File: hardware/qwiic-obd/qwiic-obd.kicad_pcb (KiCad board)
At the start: 2 copper layers, 161 parts, among them J101 I2C_STANDARD, J102 DB15_Female_HighDensity, J103 I2C_STANDARD, J601 PIC-ICSPPOLAR_LOCK, Q201 2N7002, Q202 2N7002, Q203 2N7002, Q301 2N7002, Q501 DMG2301L, Q502 DMG2301L, Q503 MMBT3906, Q504 DMG2301L, Q601 DMG2301L, Q602 2N7002, Q603 2N7002, Q604 2N7002, Q605 2N7002, Q606 2N7002, Q607 2N7002, Q608 2N7002, Q701 2N7002, Q702 2N7002, Q703 2N7002, Q704 MMBT3904, SW401 SW_Push, U201 TS5A3359DCUR, U202 TS5A3359DCUR, U203 TS5A3359DCUR, U301 TH8056KDC-AAA-008-RE, U302 MCP2557FD-xMF, U401 TCA9534, U402 MCP3423, U403 TCA9534, U404 ADM6320BX33ARJZ-R7, U405 TCA9534, U501 AP63203WU, U502 XC9142B50CMR-G, U601 LM317L_SOT-89, U602 NCS20072, U603 PIC16F15225-I/ST, U701 NCS20072, U702 SC16IS741A, U801 SC18IS602BIPW_128, U802 MCP2515-xST, X701 ASV-12.000MHZ-EJ-T, X801 ASV-12.000MHZ-EJ-T

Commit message: OK, layout v1 complete
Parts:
- removed the R301 at (127.9, 133.0)
- removed the R302 at (134.4, 123.1)
- removed R306, R409, R802, R803: 10k, Resistor_SMD:R_0805_2012Metric_Pad1.20x1.40mm_HandSolder
- removed the R617 at (189.2, 42.7)
- removed the R710 at (187.9, 70.8)
- removed U405: TCA9534, Package_SO:TSSOP-16_4.4x5mm_P0.65mm
- added J401: 1x4, Connector_PinSocket_2.54mm:PinSocket_1x04_P2.54mm_Vertical, F.Cu at (151.4, 41.2)
- added Q607: 2N7002, Package_TO_SOT_SMD:SOT-23, F.Cu at (106.7, 33.4)
- added R609: 10k, Resistor_SMD:R_0805_2012Metric_Pad1.20x1.40mm_HandSolder, B.Cu at (105.7, 32.5)
- added U204: TS5A3359DCUR, UltraLibrarian:TS5A3359DCUR, F.Cu at (55.9, 55.9)
- added U205: TS5A3359DCUR, UltraLibrarian:TS5A3359DCUR, F.Cu at (69.1, 63.5)
- C302, C503, C506, C507, C511, C604, C801, D101, D102, D103, D104, D105, D601, D604, D605, D701, Q301, Q504, Q601, R202, R204, R206, R505, R601, R701, R702, R703, R704, R706: moved to B.Cu
- Q609: renamed from Q608; moved to B.Cu
- R303: renamed from R305; moved to B.Cu
- R614: renamed from R613; moved to B.Cu
- R616: renamed from R615; moved to B.Cu
- R617: renamed from R616; moved to B.Cu
- RN403: footprint UltraLibrarian:742C163103JP -> Resistor_THT:R_Array_SIP5
- moved X801 131.6 mm to (81.8, 66.0), turned to 90 degrees
- moved L501 125.8 mm to (47.2, 21.8), turned to -90 degrees
- moved R801 124.1 mm to (94.5, 53.3)
- moved C801 120.6 mm to (88.9, 55.4), turned to 90 degrees
- moved Q501 117.7 mm to (60.4, 22.4)
- moved C508 117.0 mm to (46.2, 25.9), turned to -90 degrees
- moved C511 116.9 mm to (52.3, 23.9)
- moved U501 115.9 mm to (49.8, 21.8), turned to 90 degrees
- moved R501 114.2 mm to (54.4, 29.0), turned to -90 degrees
- moved C507 114.1 mm to (50.3, 19.8), turned to 180 degrees
- moved R505 114.0 mm to (52.3, 21.8)
- moved C509 113.8 mm to (48.3, 25.9), turned to -90 degrees
- moved Q504 113.3 mm to (48.3, 22.8), turned to 90 degrees
- moved C516 113.2 mm to (85.9, 24.9), turned to 90 degrees
- moved U802 112.7 mm to (86.4, 57.9)
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- renumbered Q607 to Q608, R303 to R301, R304 to R302, R307 to R304, R308 to R305, R609 to R610, R610 to R611, R611 to R612, R612 to R613, R614 to R615, R711 to R710
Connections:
- C302 pad 2: +5V_SW -> +5V
- C514 pad 2: +3V3 -> +5V
- C515 pad 1: +3V3 -> +5V
- C516 pad 1: +3V3 -> +5V
- C601 pad 2: VBAT -> +12V
- J102 pad 3: MS_CAN_HIGH -> MS_CAN_HI
- J102 pad 6: HS_CAN_HIGH -> HS_CAN_HI
- R506 pad 1: +3V3 -> +5V
- R614 pad 1: +5V_SW -> +5V
- RN402 pad 1: +3V3_NOSW -> ~{CAN_RX0BF}
- RN402 pad 10: Net-(RN402-Pad10) -> +3V3_NOSW
- RN402 pad 11: Net-(RN402-Pad11) -> +3V3_NOSW
- RN402 pad 12: ~{CAN_TX2RTS} -> +3V3_NOSW
- RN402 pad 13: ~{CAN_TX1RTS} -> +3V3_NOSW
- RN402 pad 14: ~{CAN_TX0RTS} -> +3V3_NOSW
- RN402 pad 15: ~{CAN_RX1BF} -> +3V3_NOSW
- RN402 pad 16: ~{CAN_RX0BF} -> +3V3_NOSW
- RN402 pad 2: +3V3_NOSW -> ~{CAN_RX1BF}
- RN402 pad 3: +3V3_NOSW -> ~{CAN_TX0RTS}
- RN402 pad 4: +3V3_NOSW -> ~{CAN_TX1RTS}
- RN402 pad 5: +3V3_NOSW -> ~{CAN_TX2RTS}
- RN402 pad 6: +3V3_NOSW -> Net-(RN402-Pad6)
- RN402 pad 7: +3V3_NOSW -> ~{RESET}
- RN402 pad 8: GND -> CAN_SOF
- RN402 pad 9: CAN_SOF -> GND
- RN403 pad 2: +3V3_NOSW -> ~{CAN_INT}
- RN403 pad 3: +3V3_NOSW -> ~{UART_INT}
- RN403 pad 4: +3V3_NOSW -> ~{SPI_INT}
- RN403 pad 5: +3V3_NOSW -> ~{J1850_INT}
- U202 pad 1: MUX_CAN_RX -> HS_CAN_HI
- U202 pad 2: MUX_CAN_RX -> MS_CAN_HI
- U202 pad 3: SW_CAN_RX -> unconnected-(U202-Pad3)
- U202 pad 7: CAN_RX -> CAN_HI
- U202 pad 8: +3V3 -> +5V
- U203 pad 1: ~{MUX_CAN_EN} -> MUX_CAN_RX
- U203 pad 2: ~{MUX_CAN_EN} -> MUX_CAN_RX
- U203 pad 3: unconnected-(U203-Pad3) -> SW_CAN_RX
- U203 pad 7: ~{CAN_EN} -> CAN_RX
- U302 pad 3: +5V_SW -> +5V
- U403 pad 10: Net-(RN402-Pad11) -> Net-(RN402-Pad6)
- U403 pad 11: Net-(RN402-Pad10) -> ~{RESET}
- U502 pad 4: +3V3 -> +5V
- U601 pad 3: VBAT -> +12V
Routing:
- net +3V3_NOSW: track 0.00 -> 189.6 mm, vias 0 -> 9
- net SDA: track 0.00 -> 183.1 mm, vias 0 -> 15
- net SCL: track 0.00 -> 182.9 mm, vias 0 -> 14
- net GND: track 0.00 -> 166.1 mm, vias 0 -> 53
- net +12V: track 0.00 -> 150.3 mm, vias 0 -> 7
- net ~{RESET}: track 0.00 -> 145.3 mm, vias 0 -> 8
- net CAN_SEL1: track 0.00 -> 99.9 mm, vias 0 -> 8
- net CAN_SEL0: track 0.00 -> 96.7 mm, vias 0 -> 8
- net J1850_BUS+: track 0.00 -> 96.4 mm, vias 0 -> 7
- net ~{CAN_INT}: track 0.00 -> 89.8 mm, vias 0 -> 5
- net PWR_CTRL: track 0.00 -> 88.3 mm, vias 0 -> 7
- net J1850_BUS-: track 0.00 -> 88.0 mm, vias 0 -> 10
- net ~{SPI_INT}: track 0.00 -> 78.9 mm, vias 0 -> 5
- net +3V3: track 0.00 -> 77.5 mm, vias 0 -> 27
- net SAE_PWM: track 0.00 -> 75.4 mm, vias 0 -> 6
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- added copper zone on In2.Cu, net +3V3
- added copper zone on In1.Cu, net +3V3_NOSW
- added copper zone on In1.Cu, net +5V
- added copper zone on B.Cu, net GND
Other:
- board outline added: 109.9 x 52.7 mm
- copper layers 2 -> 4

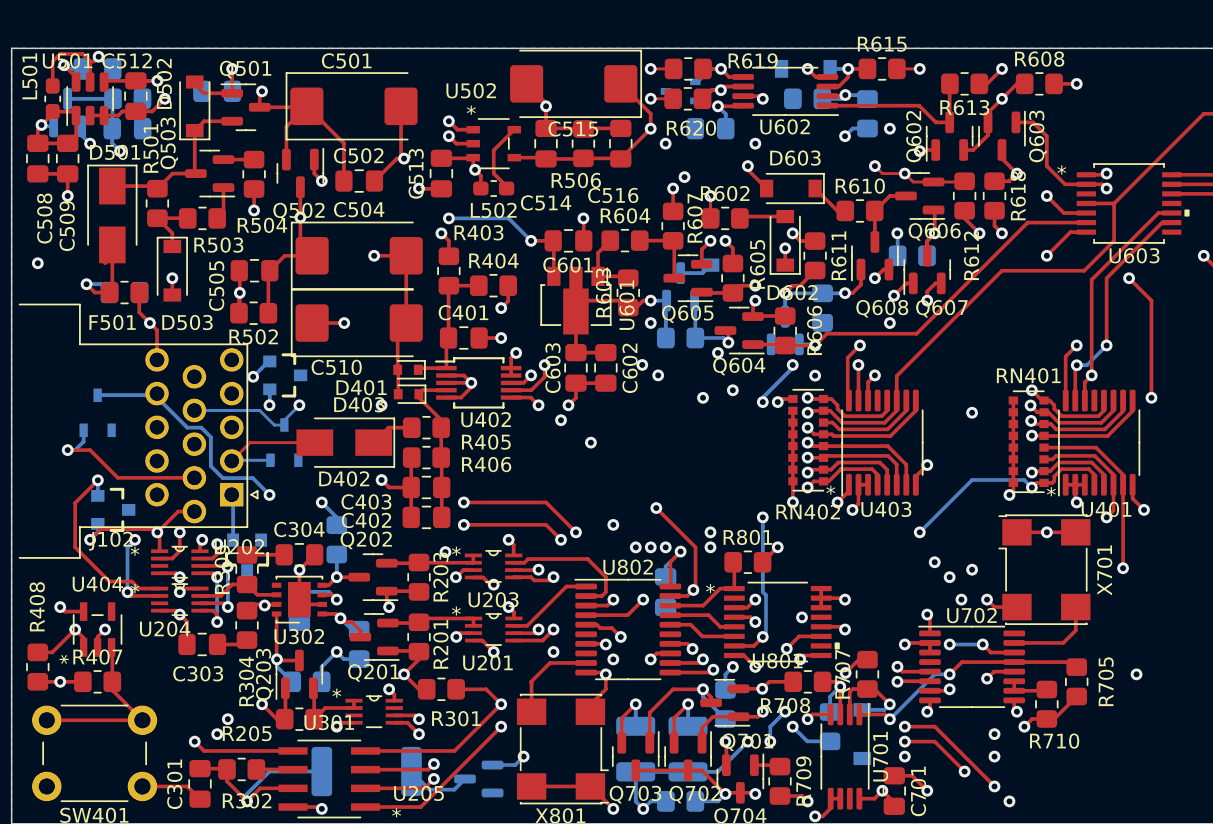
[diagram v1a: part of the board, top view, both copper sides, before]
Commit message: Get it all connected (had a few unrouted glitches)
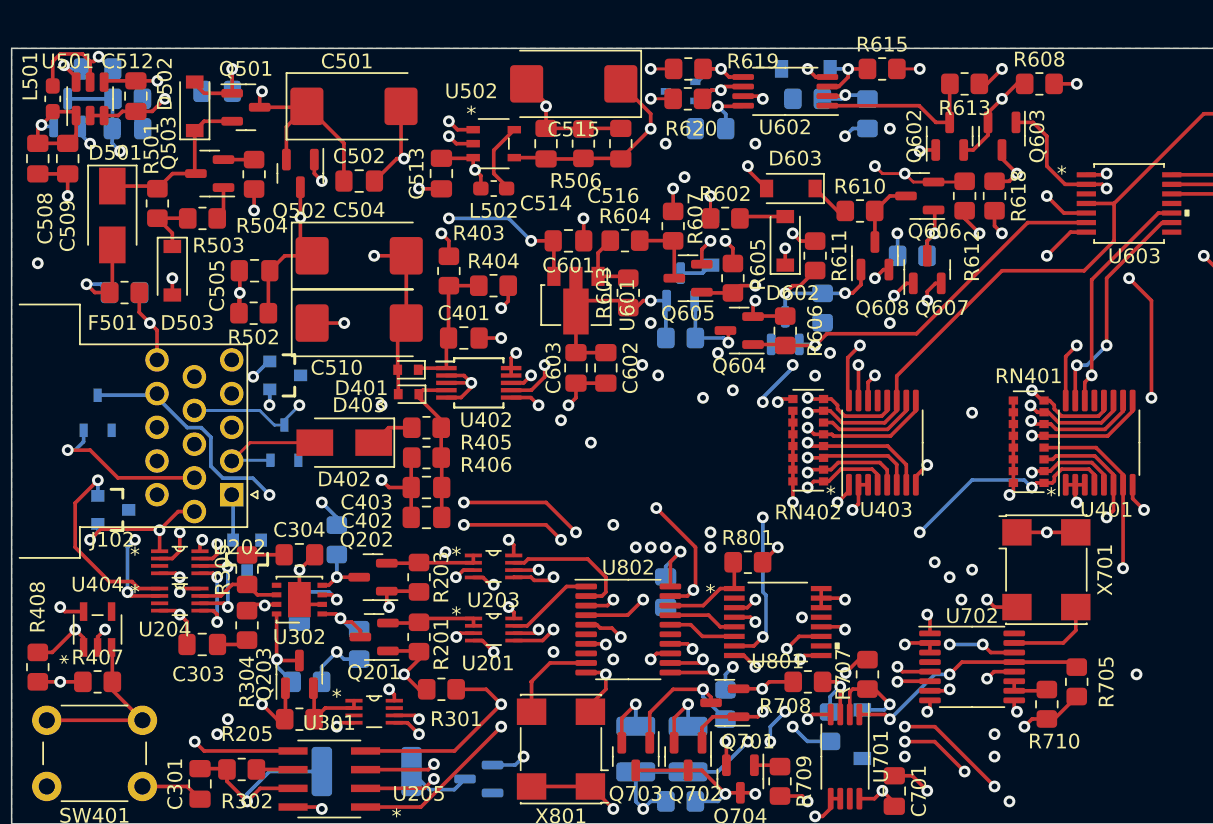
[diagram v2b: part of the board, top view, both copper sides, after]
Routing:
- net SDA: track 183.1 -> 167.7 mm
- net SCL: track 182.9 -> 168.3 mm
- net +3V3: track 77.5 -> 75.5 mm
- net GND: track 166.1 -> 164.4 mm
- net V_J1850: track 17.5 -> 16.5 mm
- net Net-(C503-Pad2): track 7.60 -> 6.90 mm
- net J1850_BUS-: track 88.0 -> 88.2 mm, vias 10 -> 11

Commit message: Fix a few tweaks
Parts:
- moved C402 4.68 mm to (76.2, 47.2), turned to 180 degrees
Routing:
- net +3V3_NOSW: track 189.6 -> 193.0 mm
- net GND: track 164.4 -> 163.6 mm, vias 53 -> 54
- net SDA: track 167.7 -> 168.3 mm, vias 15 -> 16
- net SCL: vias 14 -> 15
